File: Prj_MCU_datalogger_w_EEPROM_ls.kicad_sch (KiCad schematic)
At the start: 26 parts, among them U1 24LC1025, U2 24LC1025, U3 ATMEGA328P-AU, U4 DS1337S_, Y1 Crystal, Y2 Crystal

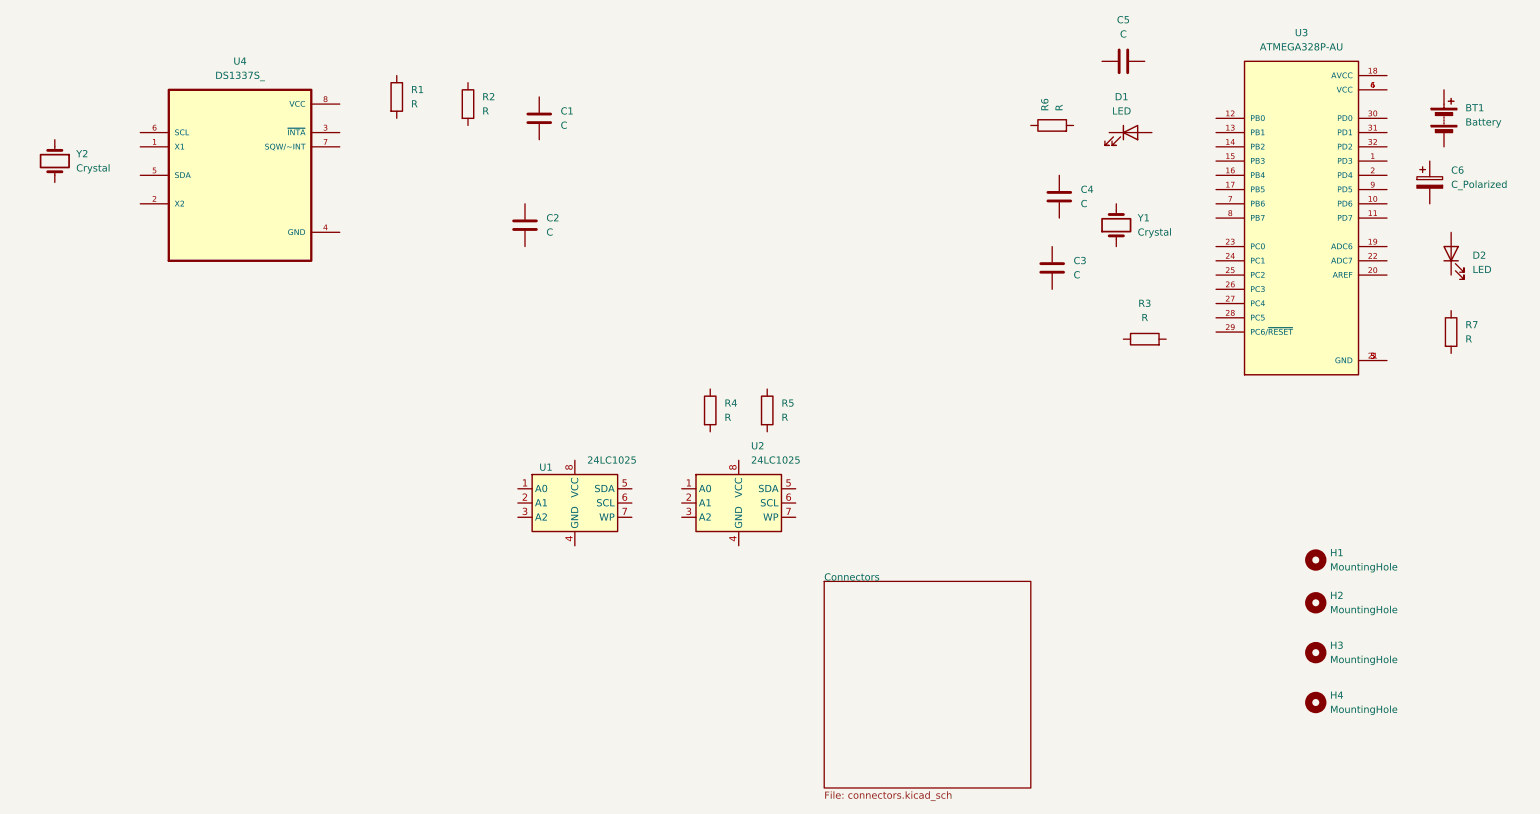
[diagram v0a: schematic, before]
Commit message: Added component values.
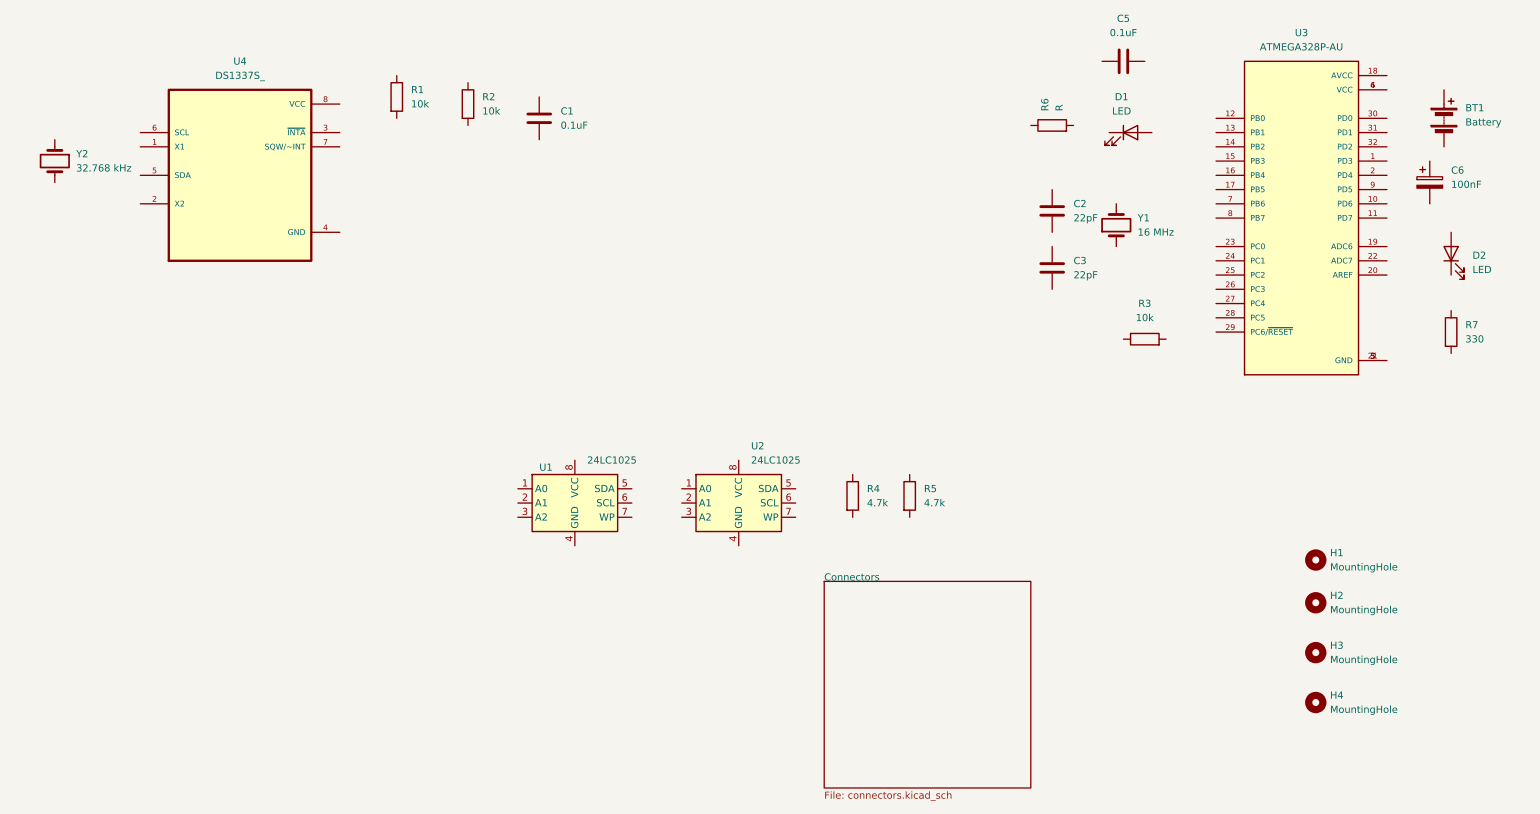
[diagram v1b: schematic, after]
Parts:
- removed C4: C, symbol Device:C
- C1, C5: value C -> 0.1uF
- C2, C3: value C -> 22pF
- C6: value C_Polarized -> 100nF
- R1, R2, R3: value R -> 10k
- R4, R5: value R -> 4.7k
- R7: value R -> 330
- Y1: value Crystal -> 16 MHz
- Y2: value Crystal -> 32.768 kHz
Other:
- moved on the sheet: C2, R4, R5
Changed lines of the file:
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@@
       (effects (font (size 1.27 1.27)))
     )
-    (property "Value" "R" (at 218.44 71.12 90)
+    (property "Value" "10k" (at 218.44 71.12 90)
       (effects (font (size 1.27 1.27)))
     )
@@
       (effects (font (size 1.27 1.27)) (justify left))
     )
-    (property "Value" "R" (at 100.33 34.29 0)
+    (property "Value" "10k" (at 100.33 34.29 0)
       (effects (font (size 1.27 1.27)) (justify left))
     )
@@
     (property "Datasheet" "~" (at 97.79 33.02 0)
       (effects (font (size 1.27 1.27)) hide)
+    )
+    (property "Purpose" "" (at 97.79 33.02 0)
+      (effects (font (size 1.27 1.27)))
     )
     (pin "2")
@@
       (effects (font (size 1.27 1.27)) (justify left))
     )
-    (property "Value" "R" (at 87.63 33.02 0)
+    (property "Value" "10k" (at 87.63 33.02 0)
       (effects (font (size 1.27 1.27)) (justify left))
     )
@@
       (effects (font (size 1.27 1.27)) hide)
     )
+    (property "Purpose" "" (at 85.09 31.75 0)
+      (effects (font (size 1.27 1.27)))
+    )
     (pin "2")
     (pin "1")
@@
       (effects (font (size 1.27 1.27)) (justify left))
     )
-    (property "Value" "R" (at 275.59 74.93 0)
+    (property "Value" "330" (at 275.59 74.93 0)
       (effects (font (size 1.27 1.27)) (justify left))
     )
@@
       (effects (font (size 1.27 1.27)) (justify left))
     )
-    (property "Value" "C" (at 114.3 36.83 0)
+    (property "Value" "0.1uF" (at 114.3 36.83 0)
       (effects (font (size 1.27 1.27)) (justify left))
     )
@@
     )
   )
-  (symbol (lib_id "Device:R") (at 140.97 87.63 0) (unit 1)
-    (in_bom yes) (on_board yes) (dnp no)
-    (property "Reference" "R4" (at 143.51 86.36 0)
-      (effects (font (size 1.27 1.27)) (justify left))
-    )
-    (property "Value" "R" (at 143.51 88.9 0)
-      (effects (font (size 1.27 1.27)) (justify left))
-    )
-    (property "Footprint" "" (at 139.192 87.63 90)
-      (effects (font (size 1.27 1.27)) hide)
-    )
-    (property "Datasheet" "~" (at 140.97 87.63 0)
+  (symbol (lib_id "Device:R") (at 166.37 102.87 0) (unit 1)
+    (in_bom yes) (on_board yes) (dnp no)
+    (property "Reference" "R4" (at 168.91 101.6 0)
+      (effects (font (size 1.27 1.27)) (justify left))
+    )
+    (property "Value" "4.7k" (at 168.91 104.14 0)
+      (effects (font (size 1.27 1.27)) (justify left))
+    )
+    (property "Footprint" "" (at 164.592 102.87 90)
+      (effects (font (size 1.27 1.27)) hide)
+    )
+    (property "Datasheet" "~" (at 166.37 102.87 0)
       (effects (font (size 1.27 1.27)) hide)
     )
@@
     )
   )
-  (symbol (lib_id "Device:R") (at 151.13 87.63 0) (unit 1)
-    (in_bom yes) (on_board yes) (dnp no)
-    (property "Reference" "R5" (at 153.67 86.36 0)
-      (effects (font (size 1.27 1.27)) (justify left))
-    )
-    (property "Value" "R" (at 153.67 88.9 0)
-      (effects (font (size 1.27 1.27)) (justify left))
-    )
-    (property "Footprint" "" (at 149.352 87.63 90)
-      (effects (font (size 1.27 1.27)) hide)
-    )
-    (property "Datasheet" "~" (at 151.13 87.63 0)
+  (symbol (lib_id "Device:R") (at 176.53 102.87 0) (unit 1)
+    (in_bom yes) (on_board yes) (dnp no)
+    (property "Reference" "R5" (at 179.07 101.6 0)
+      (effects (font (size 1.27 1.27)) (justify left))
+    )
+    (property "Value" "4.7k" (at 179.07 104.14 0)
+      (effects (font (size 1.27 1.27)) (justify left))
+    )
+    (property "Footprint" "" (at 174.752 102.87 90)
+      (effects (font (size 1.27 1.27)) hide)
+    )
+    (property "Datasheet" "~" (at 176.53 102.87 0)
       (effects (font (size 1.27 1.27)) hide)
     )
@@
     )
   )
-  (symbol (lib_id "Device:C") (at 107.95 54.61 0) (unit 1)
-    (in_bom yes) (on_board yes) (dnp no) (fields_autoplaced)
-    (property "Reference" "C2" (at 111.76 53.34 0)
-      (effects (font (size 1.27 1.27)) (justify left))
-    )
-    (property "Value" "C" (at 111.76 55.88 0)
-      (effects (font (size 1.27 1.27)) (justify left))
-    )
-    (property "Footprint" "" (at 108.9152 58.42 0)
-      (effects (font (size 1.27 1.27)) hide)
-    )
-    (property "Datasheet" "~" (at 107.95 54.61 0)
-      (effects (font (size 1.27 1.27)) hide)
+  (symbol (lib_id "Device:C") (at 201.93 52.07 0) (unit 1)
+    (in_bom yes) (on_board yes) (dnp no) (fields_autoplaced)
+    (property "Reference" "C2" (at 205.74 50.8 0)
+      (effects (font (size 1.27 1.27)) (justify left))
+    )
+    (property "Value" "22pF" (at 205.74 53.34 0)
+      (effects (font (size 1.27 1.27)) (justify left))
+    )
+    (property "Footprint" "" (at 202.8952 55.88 0)
+      (effects (font (size 1.27 1.27)) hide)
+    )
+    (property "Datasheet" "~" (at 201.93 52.07 0)
+      (effects (font (size 1.27 1.27)) hide)
+    )
+    (property "Purpose" "" (at 201.93 52.07 0)
+      (effects (font (size 1.27 1.27)))
     )
     (pin "1")
@@
       (effects (font (size 1.27 1.27)) (justify left))
     )
-    (property "Value" "C" (at 205.74 63.5 0)
+    (property "Value" "22pF" (at 205.74 63.5 0)
       (effects (font (size 1.27 1.27)) (justify left))
     )
@@
       (effects (font (size 1.27 1.27)) (justify right))
     )
-    (property "Value" "Crystal" (at 217.17 55.88 90)
+    (property "Value" "16 MHz" (at 217.17 55.88 90)
       (effects (font (size 1.27 1.27)) (justify right))
     )
@@
   (symbol (lib_id "Device:C") (at 214.63 25.4 90) (unit 1)
     (in_bom yes) (on_board yes) (dnp no) (fields_autoplaced)
-    (property "Reference" "C5" (at 214.63 18.0291 90)
-      (effects (font (size 1.27 1.27)))
-    )
-    (property "Value" "C" (at 214.63 20.5691 90)
+    (property "Reference" "C5" (at 214.63 17.78 90)
+      (effects (font (size 1.27 1.27)))
+    )
+    (property "Value" "0.1uF" (at 214.63 20.32 90)
       (effects (font (size 1.27 1.27)))
     )
@@
         (path "/d7913654-dc3e-4db0-b704-687dabf4af24"
           (reference "C5") (unit 1)
-        )
-      )
-    )
-  )
-  (symbol (lib_id "Device:C") (at 203.2 49.53 0) (unit 1)
-    (in_bom yes) (on_board yes) (dnp no) (fields_autoplaced)
-    (property "Reference" "C4" (at 207.01 48.26 0)
-      (effects (font (size 1.27 1.27)) (justify left))
-    )
-    (property "Value" "C" (at 207.01 50.8 0)
-      (effects (font (size 1.27 1.27)) (justify left))
-    )
-    (property "Footprint" "" (at 204.1652 53.34 0)
-      (effects (font (size 1.27 1.27)) hide)
-    )
-    (property "Datasheet" "~" (at 203.2 49.53 0)
-      (effects (font (size 1.27 1.27)) hide)
-    )
-    (pin "1")
-    (pin "2")
-    (instances
-      (project "Prj_MCU_datalogger_w_EEPROM_ls"
-        (path "/d7913654-dc3e-4db0-b704-687dabf4af24"
-          (reference "C4") (unit 1)
         )
       )
@@
       (effects (font (size 1.27 1.27)) (justify left))
     )
-    (property "Value" "Crystal" (at 27.94 44.45 90)
+    (property "Value" "32.768 kHz" (at 27.94 44.45 90)
       (effects (font (size 1.27 1.27)) (justify left))
     )
@@
       (effects (font (size 1.27 1.27)) hide)
     )
+    (property "Purpose" "" (at 24.13 43.18 0)
+      (effects (font (size 1.27 1.27)))
+    )
     (pin "1")
     (pin "2")
@@
       (effects (font (size 1.27 1.27)) (justify left))
     )
-    (property "Value" "C_Polarized" (at 273.05 47.371 0)
-      (effects (font (size 1.27 1.27)) (justify left))
-    )
+    (property "Value" "100nF" (at 273.05 47.371 0)
+      (effects (font (size 1.27 1.27)) (justify left))
+    )

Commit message: Completed symbol-footprint associations.
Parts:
- BT1: footprint (none) -> Connector_PinHeader_2.54mm:PinHeader_1x02_P2.54mm_Vertical
- C1, C2, C3, C5, C6: footprint (none) -> Capacitor_SMD:C_0805_2012Metric
- D1, D2: footprint (none) -> LED_SMD:LED_0805_2012Metric
- H1, H2, H3, H4: footprint (none) -> MountingHole:MountingHole_2.1mm
- R1, R2, R3, R4, R5, R6, R7: footprint (none) -> Resistor_SMD:R_0805_2012Metric
- U1, U2: footprint (none) -> Package_SO:SOIC-8_5.23x5.23mm_P1.27mm
- U3: footprint ATMEGA328P-AU:QFP80P900X900X120-32N -> Footprints:QFP80P900X900X120-32N
- U4: footprint DS1337S_:SOIC127P600X175-8N -> Footprints:SOIC127P600X175-8N
- Y1, Y2: footprint (none) -> Crystal:Crystal_SMD_5032-2Pin_5.0x3.2mm_HandSoldering
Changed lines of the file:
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@@
       (effects (font (size 1.27 1.27)))
     )
-    (property "Footprint" "" (at 218.44 76.708 90)
+    (property "Footprint" "Resistor_SMD:R_0805_2012Metric" (at 218.44 76.708 90)
       (effects (font (size 1.27 1.27)) hide)
     )
@@
       (effects (font (size 1.27 1.27)) (justify left))
     )
-    (property "Footprint" "" (at 248.92 139.7 0)
+    (property "Footprint" "MountingHole:MountingHole_2.1mm" (at 248.92 139.7 0)
       (effects (font (size 1.27 1.27)) hide)
     )
@@
       (effects (font (size 1.27 1.27)) (justify left))
     )
-    (property "Footprint" "" (at 96.012 33.02 90)
+    (property "Footprint" "Resistor_SMD:R_0805_2012Metric" (at 96.012 33.02 90)
       (effects (font (size 1.27 1.27)) hide)
     )
@@
       (effects (font (size 1.27 1.27)) (justify left))
     )
-    (property "Footprint" "" (at 116.84 104.14 0)
+    (property "Footprint" "Package_SO:SOIC-8_5.23x5.23mm_P1.27mm" (at 116.84 104.14 0)
       (effects (font (size 1.27 1.27)) hide)
     )
@@
       (effects (font (size 1.27 1.27)) (justify left))
     )
-    (property "Footprint" "" (at 83.312 31.75 90)
+    (property "Footprint" "Resistor_SMD:R_0805_2012Metric" (at 83.312 31.75 90)
       (effects (font (size 1.27 1.27)) hide)
     )
@@
       (effects (font (size 1.27 1.27)) (justify left))
     )
-    (property "Footprint" "" (at 248.92 114.3 0)
+    (property "Footprint" "MountingHole:MountingHole_2.1mm" (at 248.92 114.3 0)
       (effects (font (size 1.27 1.27)) hide)
     )
@@
       (effects (font (size 1.27 1.27)) (justify left))
     )
-    (property "Footprint" "" (at 271.272 73.66 90)
+    (property "Footprint" "Resistor_SMD:R_0805_2012Metric" (at 271.272 73.66 90)
       (effects (font (size 1.27 1.27)) hide)
     )
@@
       (effects (font (size 1.27 1.27)) (justify left))
     )
-    (property "Footprint" "" (at 111.4552 39.37 0)
+    (property "Footprint" "Capacitor_SMD:C_0805_2012Metric" (at 111.4552 39.37 0)
       (effects (font (size 1.27 1.27)) hide)
     )
@@
       (effects (font (size 1.27 1.27)) (justify left))
     )
-    (property "Footprint" "" (at 164.592 102.87 90)
+    (property "Footprint" "Resistor_SMD:R_0805_2012Metric" (at 164.592 102.87 90)
       (effects (font (size 1.27 1.27)) hide)
     )
@@
       (effects (font (size 1.27 1.27)))
     )
-    (property "Footprint" "" (at 215.9 38.1 0)
+    (property "Footprint" "LED_SMD:LED_0805_2012Metric" (at 215.9 38.1 0)
       (effects (font (size 1.27 1.27)) hide)
     )
@@
       (effects (font (size 1.27 1.27)) (justify left))
     )
-    (property "Footprint" "" (at 248.92 121.92 0)
+    (property "Footprint" "MountingHole:MountingHole_2.1mm" (at 248.92 121.92 0)
       (effects (font (size 1.27 1.27)) hide)
     )
@@
       (effects (font (size 1.27 1.27)) (justify left))
     )
-    (property "Footprint" "" (at 201.93 38.608 90)
+    (property "Footprint" "Resistor_SMD:R_0805_2012Metric" (at 201.93 38.608 90)
       (effects (font (size 1.27 1.27)) hide)
     )
@@
       (effects (font (size 1.27 1.27)) (justify left))
     )
-    (property "Footprint" "" (at 174.752 102.87 90)
+    (property "Footprint" "Resistor_SMD:R_0805_2012Metric" (at 174.752 102.87 90)
       (effects (font (size 1.27 1.27)) hide)
     )
@@
       (effects (font (size 1.27 1.27)))
     )
-    (property "Footprint" "ATMEGA328P-AU:QFP80P900X900X120-32N" (at 246.38 53.34 0)
+    (property "Footprint" "Footprints:QFP80P900X900X120-32N" (at 246.38 53.34 0)
       (effects (font (size 1.27 1.27)) (justify bottom) hide)
     )
@@
       (effects (font (size 1.27 1.27)))
     )
-    (property "Footprint" "DS1337S_:SOIC127P600X175-8N" (at 57.15 45.72 0)
+    (property "Footprint" "Footprints:SOIC127P600X175-8N" (at 57.15 45.72 0)
       (effects (font (size 1.27 1.27)) (justify bottom) hide)
     )
@@
       (effects (font (size 1.27 1.27)) (justify right))
     )
-    (property "Footprint" "" (at 273.05 59.69 0)
+    (property "Footprint" "LED_SMD:LED_0805_2012Metric" (at 273.05 59.69 0)
       (effects (font (size 1.27 1.27)) hide)
     )
@@
       (effects (font (size 1.27 1.27)) (justify left))
     )
-    (property "Footprint" "" (at 202.8952 55.88 0)
+    (property "Footprint" "Capacitor_SMD:C_0805_2012Metric" (at 202.8952 55.88 0)
       (effects (font (size 1.27 1.27)) hide)
     )
@@
       (effects (font (size 1.27 1.27)) (justify left))
     )
-    (property "Footprint" "" (at 271.78 34.036 90)
+    (property "Footprint" "Connector_PinHeader_2.54mm:PinHeader_1x02_P2.54mm_Vertical" (at 271.78 34.036 90)
       (effects (font (size 1.27 1.27)) hide)
     )
@@
       (effects (font (size 1.27 1.27)) (justify left))
     )
-    (property "Footprint" "" (at 202.8952 66.04 0)
+    (property "Footprint" "Capacitor_SMD:C_0805_2012Metric" (at 202.8952 66.04 0)
       (effects (font (size 1.27 1.27)) hide)
     )
@@
       (effects (font (size 1.27 1.27)) (justify right))
     )
-    (property "Footprint" "" (at 213.36 54.61 0)
+    (property "Footprint" "Crystal:Crystal_SMD_5032-2Pin_5.0x3.2mm_HandSoldering" (at 213.36 54.61 0)
       (effects (font (size 1.27 1.27)) hide)
     )
@@
       (effects (font (size 1.27 1.27)) (justify left))
     )
-    (property "Footprint" "" (at 248.92 130.81 0)
+    (property "Footprint" "MountingHole:MountingHole_2.1mm" (at 248.92 130.81 0)
       (effects (font (size 1.27 1.27)) hide)
     )
@@
       (effects (font (size 1.27 1.27)))
     )
-    (property "Footprint" "" (at 218.44 24.4348 0)
+    (property "Footprint" "Capacitor_SMD:C_0805_2012Metric" (at 218.44 24.4348 0)
       (effects (font (size 1.27 1.27)) hide)
     )
@@
       (effects (font (size 1.27 1.27)) (justify left))
     )
-    (property "Footprint" "" (at 146.05 104.14 0)
+    (property "Footprint" "Package_SO:SOIC-8_5.23x5.23mm_P1.27mm" (at 146.05 104.14 0)
       (effects (font (size 1.27 1.27)) hide)
     )
@@
       (effects (font (size 1.27 1.27)) (justify left))
     )
-    (property "Footprint" "" (at 24.13 43.18 0)
+    (property "Footprint" "Crystal:Crystal_SMD_5032-2Pin_5.0x3.2mm_HandSoldering" (at 24.13 43.18 0)
       (effects (font (size 1.27 1.27)) hide)
     )
@@
       (effects (font (size 1.27 1.27)) (justify left))
     )
-    (property "Footprint" "" (at 270.2052 50.8 0)
-      (effects (font (size 1.27 1.27)) hide)
-    )
+    (property "Footprint" "Capacitor_SMD:C_0805_2012Metric" (at 270.2052 50.8 0)
+      (effects (font (size 1.27 1.27)) hide)
+    )
